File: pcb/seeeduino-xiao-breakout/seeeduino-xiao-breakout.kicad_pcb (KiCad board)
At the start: 2 copper layers, 69.5 x 69.5 mm, 24 parts, among them J1 Conn_01x01_hole, J10 Conn_01x01_hole, J11 Conn_01x01_hole, J12 Conn_01x01_hole, J13 Conn_01x01_hole, J14 Conn_01x01_hole, J2 Conn_01x01_hole, J3 Conn_01x01_hole, J4 Conn_01x01_hole, J5 Conn_01x01_hole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

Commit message: make edge connector hole larger for alligator clips
Previously, the hole was a little small for the alligator clips to
actually latch onto. It wasn't a big deal, but hopefully the new
slightly larger oval hole works better.
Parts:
- R1: value 220 -> 470
- R2: value 100 -> 200
- turned J10 to 7 degrees
- turned J3 to 74.5 degrees

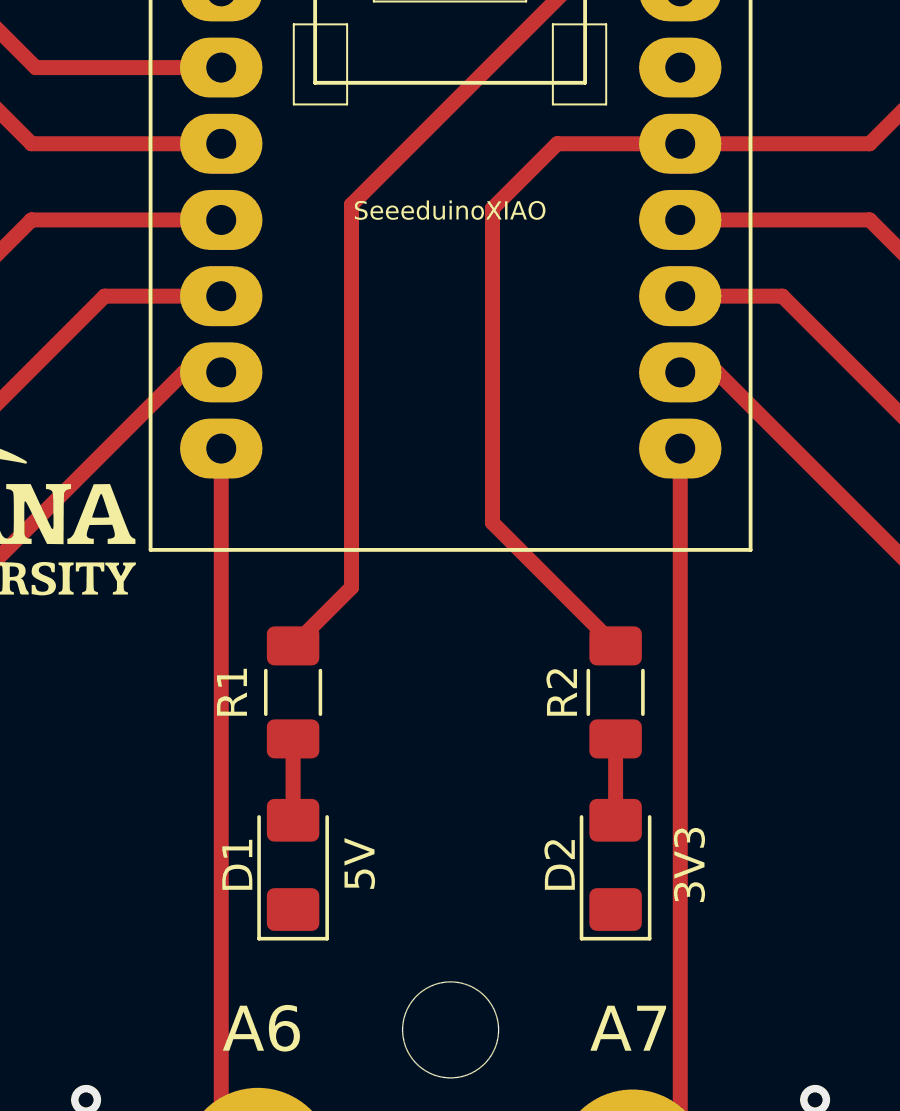
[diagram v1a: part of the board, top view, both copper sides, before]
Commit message: update seeduino footprint type and add spot for name on silkscreen
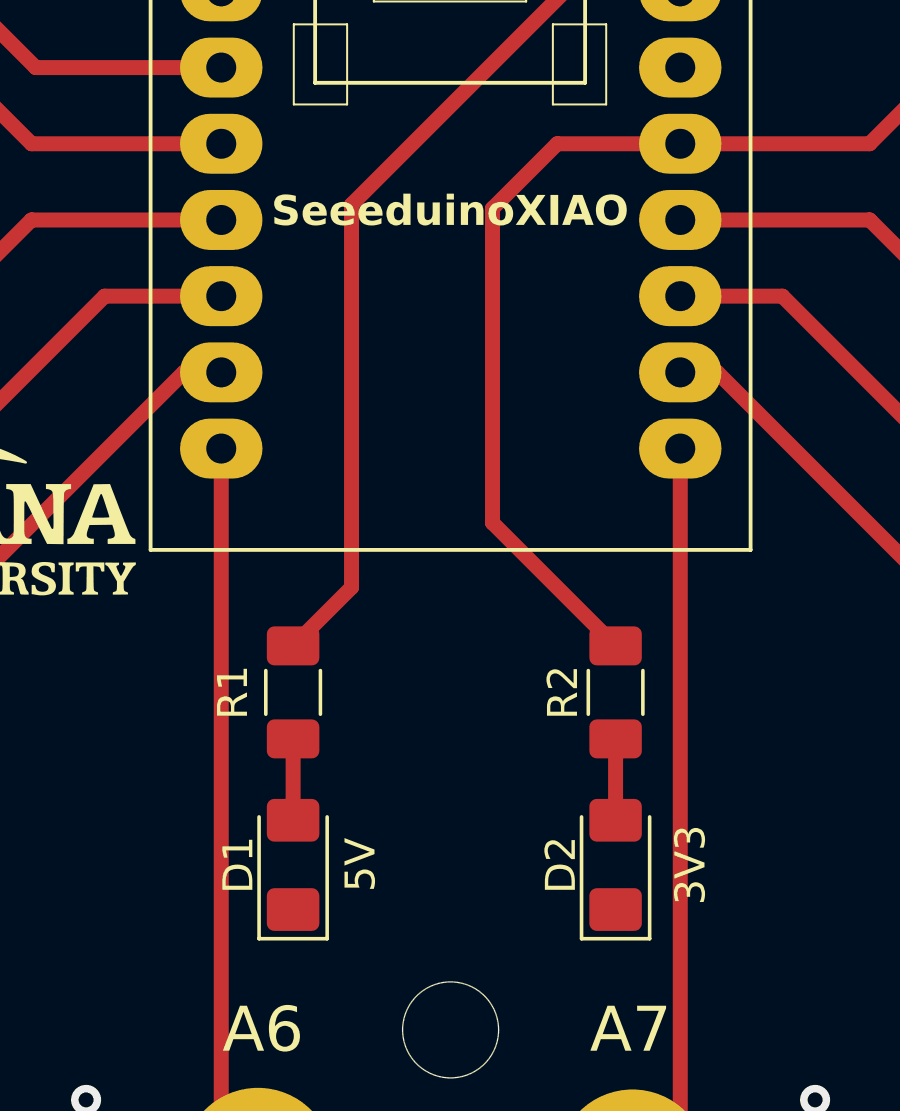
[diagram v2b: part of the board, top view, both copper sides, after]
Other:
- board text added: "This board belongs to:"
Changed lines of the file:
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@@
 			(effects
 				(font
-					(size 0.6096 0.6096)
-					(thickness 0.0762)
+					(size 1 1)
+					(thickness 0.2)
+					(bold yes)
 				)
 			)
@@
 		(sheetname "Root")
 		(sheetfile "seeeduino-xiao-breakout.kicad_sch")
-		(attr smd)
+		(attr through_hole)
 		(fp_line
 			(start -10 -9.76381)
@@
 			(pintype "passive")
 		)
-		(model "${KICAD6_3DMODEL_DIR}/LED_SMD.3dshapes/LED_1206_3216Metric.wrl"
+		(model "${KICAD8_3DMODEL_DIR}/LED_SMD.3dshapes/LED_1206_3216Metric.wrl"
 			(offset
 				(xyz 0 0 0)
@@
 			(size 1.3 1.75)
 			(layers "F.Cu" "F.Paste" "F.Mask")
-			(roundrect_rratio 0.1923076923)
+			(roundrect_rratio 0.192308)
 			(net 3 "+5V")
 			(pintype "passive")
@@
 			(size 1.3 1.75)
 			(layers "F.Cu" "F.Paste" "F.Mask")
-			(roundrect_rratio 0.1923076923)
+			(roundrect_rratio 0.192308)
 			(net 4 "Net-(D1-A)")
 			(pintype "passive")
 		)
-		(model "${KICAD6_3DMODEL_DIR}/Resistor_SMD.3dshapes/R_1206_3216Metric.wrl"
+		(model "${KICAD8_3DMODEL_DIR}/Resistor_SMD.3dshapes/R_1206_3216Metric.wrl"
 			(offset
 				(xyz 0 0 0)
@@
 			(size 1.425 1.75)
 			(layers "F.Cu" "F.Paste" "F.Mask")
-			(roundrect_rratio 0.1754392982)
+			(roundrect_rratio 0.175439)
 			(net 2 "GND")
 			(pinfunction "K")
@@
 			(size 1.425 1.75)
 			(layers "F.Cu" "F.Paste" "F.Mask")
-			(roundrect_rratio 0.1754392982)
+			(roundrect_rratio 0.175439)
 			(net 5 "Net-(D2-A)")
 			(pinfunction "A")
 			(pintype "passive")
 		)
-		(model "${KICAD6_3DMODEL_DIR}/LED_SMD.3dshapes/LED_1206_3216Metric.wrl"
+		(model "${KICAD8_3DMODEL_DIR}/LED_SMD.3dshapes/LED_1206_3216Metric.wrl"
 			(offset
 				(xyz 0 0 0)
@@
 			(size 1.3 1.75)
 			(layers "F.Cu" "F.Paste" "F.Mask")
-			(roundrect_rratio 0.1923076923)
+			(roundrect_rratio 0.192308)
 			(net 1 "+3V3")
 			(pintype "passive")
@@
 			(size 1.3 1.75)
 			(layers "F.Cu" "F.Paste" "F.Mask")
-			(roundrect_rratio 0.1923076923)
+			(roundrect_rratio 0.192308)
 			(net 5 "Net-(D2-A)")
 			(pintype "passive")
 		)
-		(model "${KICAD6_3DMODEL_DIR}/Resistor_SMD.3dshapes/R_1206_3216Metric.wrl"
+		(model "${KICAD8_3DMODEL_DIR}/Resistor_SMD.3dshapes/R_1206_3216Metric.wrl"
 			(offset
 				(xyz 0 0 0)
@@
 		)
 	)
+	(gr_rect
+		(start 115.9 117.9)
+		(end 158.9 124.4)
+		(stroke
+			(width 0.15)
+			(type default)
+		)
+		(fill solid)
+		(layer "B.SilkS")
+	)
 	(gr_circle
 		(center 137.4 101.65)
@@
 		(layer "Edge.Cuts")
 	)
+	(gr_text "This board belongs to:"
+		(at 154.65 116.9 0)
+		(layer "B.SilkS")
+		(effects
+			(font
+				(size 2 2)
+				(thickness 0.3)
+			)
+			(justify left bottom mirror)
+		)
+	)
 	(gr_text "A1"

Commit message: add qr code and url
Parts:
- added QR*****: https://github.com/BMW-lab-MSU/game-controller-summer-camp, lib:github-repo-qrcode, B.Cu at (137.4, 85.2)
- added REF**: OSHW-Logo_11.4x12mm_SilkScreen, Symbol:OSHW-Logo_11.4x12mm_SilkScreen, B.Cu at (137.4, 101.7)
